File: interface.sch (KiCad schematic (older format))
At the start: 13 parts

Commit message: sch has been finished
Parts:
- removed P?: CONN_10, symbol CONN_10
- removed P?: CONN_01X02, symbol CONN_01X02
- added P11: CONN_1x2, symbol CONN_1x2
- added P6: CONN_10, symbol CONN_10
- P10, P14, P15: renamed from P?; symbol CONN_01X02 -> CONN_01X02-RESCUE-BBBCanFly
- gave numbers to parts that had none: 8
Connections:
- net labels added: I2C2_SCL, LCD_DATA5, MMC1_DAT5, P8, P9, SPI1_DI
- net labels removed: CSN, ECAP0, FSYNC, GDO0, GDO2, GPIO_122, INT, SCL, SCLK, SDA, SI, SO, SPI0_SCLK, VCC
- wire segments 133 -> 143
- no-connect marks 0 -> 72
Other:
- moved on the sheet: P12, P13, P7, P8, P9

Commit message: pcb finished.
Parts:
- removed P10, P14, P15: CONN_01X02, symbol CONN_01X02-RESCUE-BBBCanFly
- removed P11: CONN_1x2, symbol CONN_1x2
- added R6: 200K, Resistors_SMD:R_0805, symbol R
- added R7: 30K, Resistors_SMD:R_0805, symbol R
- P12, P13, P8, P9: footprint (none) -> Pin_Headers:Pin_Header_Straight_1x03
- P3, P4: footprint (none) -> Pin_Headers:Pin_Header_Straight_2x23
- P5: footprint (none) -> Pin_Headers:Pin_Header_Straight_2x05
- P6: footprint (none) -> Pin_Headers:Pin_Header_Straight_1x10
- P7: footprint (none) -> Pin_Headers:Pin_Header_Straight_1x04
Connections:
- net labels added: GPIO_26
- wire segments 143 -> 132
- no-connect marks 72 -> 71
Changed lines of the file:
@@
 GPIO_44
 Text Label 4600 1300 0    60   ~ 0
-EHRPWM1A
+GPIO_26
 Text Label 4600 1400 0    60   ~ 0
 GPIO_46
@@
 F 0 "P7" V 8200 950 50  0000 C CNN
 F 1 "CONN_4" V 8300 950 50  0000 C CNN
-F 2 "" H 8250 950 60  0000 C CNN
+F 2 "Pin_Headers:Pin_Header_Straight_1x04" H 8250 950 60  0001 C CNN
 F 3 "" H 8250 950 60  0000 C CNN
 	1    8250 950
@@
 F 0 "P3" H 1650 3000 50  0000 C CNN
 F 1 "CONN_02X23" V 1650 1800 50  0000 C CNN
-F 2 "" H 1650 950 50  0000 C CNN
+F 2 "Pin_Headers:Pin_Header_Straight_2x23" H 1650 950 50  0001 C CNN
 F 3 "" H 1650 950 50  0000 C CNN
 	1    1650 1800
@@
 F 0 "P4" H 4300 3000 50  0000 C CNN
 F 1 "CONN_02X23" V 4300 1800 50  0000 C CNN
-F 2 "" H 4300 950 50  0000 C CNN
+F 2 "Pin_Headers:Pin_Header_Straight_2x23" H 4300 950 50  0001 C CNN
 F 3 "" H 4300 950 50  0000 C CNN
 	1    4300 1800
@@
 F 0 "P5" H 6550 1200 50  0000 C CNN
 F 1 "CONN_02X05" H 6550 600 50  0001 C CNN
-F 2 "" H 6550 -300 50  0000 C CNN
+F 2 "Pin_Headers:Pin_Header_Straight_2x05" H 6550 -300 50  0001 C CNN
 F 3 "" H 6550 -300 50  0000 C CNN
 	1    6550 900
@@
 Wire Notes Line
 	8400 1500 8400 550
-$Comp
-L CONN_01X02-RESCUE-BBBCanFly P10
-U 1 1 57651A73
-P 9950 850
-AR Path="/57651A73" Ref="P10"  Part="1"
-AR Path="/570FB5F8/57651A73" Ref="P10"  Part="1"
-F 0 "P10" H 9950 1000 50  0000 C CNN
-F 1 "CONN_01X02" V 10050 850 50  0000 C CNN
-F 2 "" H 9950 850 50  0000 C CNN
-F 3 "" H 9950 850 50  0000 C CNN
-	1    9950 850
-	1    0    0    -1
-$EndComp
-$Comp
-L CONN_01X02-RESCUE-BBBCanFly P15
-U 1 1 57651C86
-P 10750 850
-AR Path="/57651C86" Ref="P15"  Part="1"
-AR Path="/570FB5F8/57651C86" Ref="P15"  Part="1"
-F 0 "P15" H 10750 1000 50  0000 C CNN
-F 1 "CONN_01X02" V 10850 850 50  0000 C CNN
-F 2 "" H 10750 850 50  0000 C CNN
-F 3 "" H 10750 850 50  0000 C CNN
-	1    10750 850
-	1    0    0    -1
-$EndComp
-$Comp
-L CONN_01X02-RESCUE-BBBCanFly P14
-U 1 1 57651D39
-P 10700 1450
-AR Path="/57651D39" Ref="P14"  Part="1"
-AR Path="/570FB5F8/57651D39" Ref="P14"  Part="1"
-F 0 "P14" H 10700 1600 50  0000 C CNN
-F 1 "CONN_01X02" V 10800 1450 50  0000 C CNN
-F 2 "" H 10700 1450 50  0000 C CNN
-F 3 "" H 10700 1450 50  0000 C CNN
-	1    10700 1450
-	1    0    0    -1
-$EndComp
-$Comp
-L +24V #PWR7
-U 1 1 57651D88
-P 9550 750
-F 0 "#PWR7" H 9550 600 50  0001 C CNN
-F 1 "+24V" H 9550 890 50  0000 C CNN
-F 2 "" H 9550 750 50  0000 C CNN
-F 3 "" H 9550 750 50  0000 C CNN
-	1    9550 750
-	1    0    0    -1
-$EndComp
-$Comp
-L +24V #PWR15
-U 1 1 57651DAE
-P 10350 1350
-F 0 "#PWR15" H 10350 1200 50  0001 C CNN
-F 1 "+24V" H 10350 1490 50  0000 C CNN
-F 2 "" H 10350 1350 50  0000 C CNN
-F 3 "" H 10350 1350 50  0000 C CNN
-	1    10350 1350
-	1    0    0    -1
-$EndComp
-$Comp
-L +24V #PWR13
-U 1 1 57651E68
-P 10350 750
-F 0 "#PWR13" H 10350 600 50  0001 C CNN
-F 1 "+24V" H 10350 890 50  0000 C CNN
-F 2 "" H 10350 750 50  0000 C CNN
-F 3 "" H 10350 750 50  0000 C CNN
-	1    10350 750
-	1    0    0    -1
-$EndComp
-$Comp
-L +24V #PWR9
-U 1 1 57651E8E
-P 9550 1350
-F 0 "#PWR9" H 9550 1200 50  0001 C CNN
-F 1 "+24V" H 9550 1490 50  0000 C CNN
-F 2 "" H 9550 1350 50  0000 C CNN
-F 3 "" H 9550 1350 50  0000 C CNN
-	1    9550 1350
-	1    0    0    -1
-$EndComp
-Wire Wire Line
-	9450 800  9750 800
-Wire Wire Line
-	10350 800  10550 800
-Wire Wire Line
-	10500 1400 10350 1400
-Wire Wire Line
-	9550 1400 9750 1400
-$Comp
-L GND #PWR8
-U 1 1 57653080
-P 9550 950
-F 0 "#PWR8" H 9550 700 50  0001 C CNN
-F 1 "GND" H 9550 800 50  0000 C CNN
-F 2 "" H 9550 950 50  0000 C CNN
-F 3 "" H 9550 950 50  0000 C CNN
-	1    9550 950
-	1    0    0    -1
-$EndComp
-$Comp
-L GND #PWR14
-U 1 1 576530D8
-P 10350 950
-F 0 "#PWR14" H 10350 700 50  0001 C CNN
-F 1 "GND" H 10350 800 50  0000 C CNN
-F 2 "" H 10350 950 50  0000 C CNN
-F 3 "" H 10350 950 50  0000 C CNN
-	1    10350 950
-	1    0    0    -1
-$EndComp
-$Comp
-L GND #PWR16
-U 1 1 576530FE
-P 10350 1550
-F 0 "#PWR16" H 10350 1300 50  0001 C CNN
-F 1 "GND" H 10350 1400 50  0000 C CNN
-F 2 "" H 10350 1550 50  0000 C CNN
-F 3 "" H 10350 1550 50  0000 C CNN
-	1    10350 1550
-	1    0    0    -1
-$EndComp
-$Comp
-L GND #PWR10
-U 1 1 57653124
-P 9550 1550
-F 0 "#PWR10" H 9550 1300 50  0001 C CNN
-F 1 "GND" H 9550 1400 50  0000 C CNN
-F 2 "" H 9550 1550 50  0000 C CNN
-F 3 "" H 9550 1550 50  0000 C CNN
-	1    9550 1550
-	1    0    0    -1
-$EndComp
-Wire Wire Line
-	10550 900  10350 900
-Wire Wire Line
-	9550 900  9750 900
-Wire Wire Line
-	9750 1500 9550 1500
-Wire Wire Line
-	10350 1500 10500 1500
 $Comp
 L CONN_01X03 P8
@@
 F 0 "P8" H 8800 2400 50  0000 C CNN
 F 1 "CONN_01X03" V 8900 2200 50  0000 C CNN
-F 2 "" H 8800 2200 50  0000 C CNN
+F 2 "Pin_Headers:Pin_Header_Straight_1x03" H 8800 2200 50  0001 C CNN
 F 3 "" H 8800 2200 50  0000 C CNN
 	1    8800 2200
@@
 F 0 "P12" H 10150 2400 50  0000 C CNN
 F 1 "CONN_01X03" V 10250 2200 50  0000 C CNN
-F 2 "" H 10150 2200 50  0000 C CNN
+F 2 "Pin_Headers:Pin_Header_Straight_1x03" H 10150 2200 50  0001 C CNN
 F 3 "" H 10150 2200 50  0000 C CNN
 	1    10150 2200
@@
 F 0 "P9" H 8800 3200 50  0000 C CNN
 F 1 "CONN_01X03" V 8900 3000 50  0000 C CNN
-F 2 "" H 8800 3000 50  0000 C CNN
+F 2 "Pin_Headers:Pin_Header_Straight_1x03" H 8800 3000 50  0001 C CNN
 F 3 "" H 8800 3000 50  0000 C CNN
 	1    8800 3000
@@
 F 0 "P13" H 10150 3200 50  0000 C CNN
 F 1 "CONN_01X03" V 10250 3000 50  0000 C CNN
-F 2 "" H 10150 3000 50  0000 C CNN
+F 2 "Pin_Headers:Pin_Header_Straight_1x03" H 10150 3000 50  0001 C CNN
 F 3 "" H 10150 3000 50  0000 C CNN
 	1    10150 3000
@@
 $EndComp
 $Comp
-L GND #PWR5
+L GND #PWR04
 U 1 1 5765358A
 P 8400 2350
-F 0 "#PWR5" H 8400 2100 50  0001 C CNN
+F 0 "#PWR04" H 8400 2100 50  0001 C CNN
 F 1 "GND" H 8400 2200 50  0000 C CNN
 F 2 "" H 8400 2350 50  0000 C CNN
@@
 $EndComp
 $Comp
-L GND #PWR11
+L GND #PWR05
 U 1 1 576535BC
 P 9800 2350
-F 0 "#PWR11" H 9800 2100 50  0001 C CNN
+F 0 "#PWR05" H 9800 2100 50  0001 C CNN
 F 1 "GND" H 9800 2200 50  0000 C CNN
 F 2 "" H 9800 2350 50  0000 C CNN
@@
 $EndComp
 $Comp
-L GND #PWR6
+L GND #PWR06
 U 1 1 576537B9
 P 8450 3150
-F 0 "#PWR6" H 8450 2900 50  0001 C CNN
+F 0 "#PWR06" H 8450 2900 50  0001 C CNN
 F 1 "GND" H 8450 3000 50  0000 C CNN
 F 2 "" H 8450 3150 50  0000 C CNN
@@
 $EndComp
 $Comp
-L GND #PWR12
+L GND #PWR07
 U 1 1 576537EB
 P 9800 3100
-F 0 "#PWR12" H 9800 2850 50  0001 C CNN
+F 0 "#PWR07" H 9800 2850 50  0001 C CNN
 F 1 "GND" H 9800 2950 50  0000 C CNN
 F 2 "" H 9800 3100 50  0000 C CNN
@@
 Text Label 8100 2900 0    60   ~ 0
 EHRPWM2A
-Text HLabel 9450 800  0    60   Input ~ 0
-24V
 Text Label 4250 3100 0    60   ~ 0
 P8
@@
 ECAPPWM0
 $Comp
-L GND #PWR4
+L GND #PWR08
 U 1 1 57B1CADA
 P 6250 1900
-F 0 "#PWR4" H 6250 1650 50  0001 C CNN
+F 0 "#PWR08" H 6250 1650 50  0001 C CNN
 F 1 "GND" H 6250 1750 50  0000 C CNN
 F 2 "" H 6250 1900 50  0000 C CNN
@@
 NoConn ~ 750  2400
 NoConn ~ 750  2500
-NoConn ~ 750  2600
 NoConn ~ 750  2700
 NoConn ~ 2550 2600
@@
 	8400 2350 8400 2300
 Wire Wire Line
-	9550 950  9550 900
-Wire Wire Line
-	10350 900  10350 950
-Wire Wire Line
 	8450 3100 8450 3150
 Wire Wire Line
 	9800 2300 9800 2350
-Wire Wire Line
-	9550 1400 9550 1350
-Wire Wire Line
-	9550 1500 9550 1550
-Wire Wire Line
-	10350 1550 10350 1500
-Wire Wire Line
-	10350 1400 10350 1350
-Wire Wire Line
-	9550 800  9550 750
-Wire Wire Line
-	10350 800  10350 750
 Text Label 6350 2700 0    60   ~ 0
 DGND
 Wire Wire Line
 	6750 2700 6350 2700
-Connection ~ 9550 800
-$Comp
-L CONN_1x2 P11
-U 1 1 57B257AC
-P 10000 1300
-F 0 "P11" H 9950 1300 60  0000 C CNN
-F 1 "CONN_1x2" V 10100 1150 60  0000 C CNN
-F 2 "" H 10000 1300 60  0000 C CNN
-F 3 "" H 10000 1300 60  0000 C CNN
-	1    10000 1300
-	1    0    0    -1
-$EndComp
 $Comp
 L CONN_10 P6
@@
 F 0 "P6" V 6950 1250 60  0000 C CNN
 F 1 "CONN_10" V 7050 1250 60  0000 C CNN
-F 2 "" H 7000 1750 60  0000 C CNN
+F 2 "Pin_Headers:Pin_Header_Straight_1x10" H 7000 1750 60  0001 C CNN
 F 3 "" H 7000 1750 60  0000 C CNN
 	1    7000 1750
 	1    0    0    -1
 $EndComp
+$Comp
+L +24V #PWR09
+U 1 1 57CD415B
+P 9000 700
+F 0 "#PWR09" H 9000 550 50  0001 C CNN
+F 1 "+24V" H 9000 840 50  0000 C CNN
+F 2 "" H 9000 700 50  0000 C CNN
+F 3 "" H 9000 700 50  0000 C CNN
+	1    9000 700
+	1    0    0    -1
+$EndComp
+$Comp
+L GND #PWR010
+U 1 1 57CD418D
+P 9000 1550
+F 0 "#PWR010" H 9000 1300 50  0001 C CNN
+F 1 "GND" H 9000 1400 50  0000 C CNN
+F 2 "" H 9000 1550 50  0000 C CNN
+F 3 "" H 9000 1550 50  0000 C CNN
+	1    9000 1550
+	1    0    0    -1
+$EndComp
+$Comp
+L R R6
+U 1 1 57CD41E5
+P 9000 950
+F 0 "R6" V 9080 950 50  0000 C CNN
+F 1 "200K" V 9000 950 50  0000 C CNN
+F 2 "Resistors_SMD:R_0805" V 8930 950 50  0001 C CNN
+F 3 "" H 9000 950 50  0000 C CNN
+	1    9000 950
+	1    0    0    -1
+$EndComp
+$Comp
+L R R7
+U 1 1 57CD4260
+P 9000 1350
+F 0 "R7" V 9080 1350 50  0000 C CNN
+F 1 "30K" V 9000 1350 50  0000 C CNN
+F 2 "Resistors_SMD:R_0805" V 8930 1350 50  0001 C CNN
+F 3 "" H 9000 1350 50  0000 C CNN
+	1    9000 1350
+	1    0    0    -1
+$EndComp
+Wire Wire Line
+	9000 700  9000 800
+Wire Wire Line
+	9000 1100 9000 1200
+Wire Wire Line
+	9000 1500 9000 1550
+Wire Wire Line
+	9000 1150 8650 1150
+Connection ~ 9000 1150
+Text Label 8650 1150 0    60   ~ 0
+AIN0
+Wire Wire Line
+	8750 750  9000 750
+Connection ~ 9000 750
+Text HLabel 8750 750  0    60   Input ~ 0
+24V
 $EndSCHEMATC

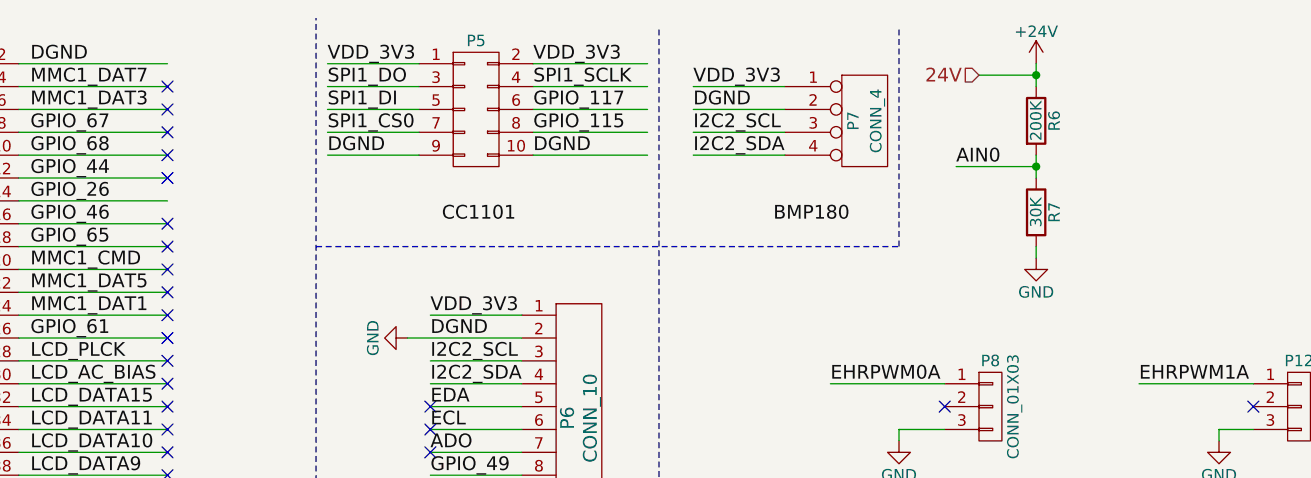
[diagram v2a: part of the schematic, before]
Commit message: modified power supply program
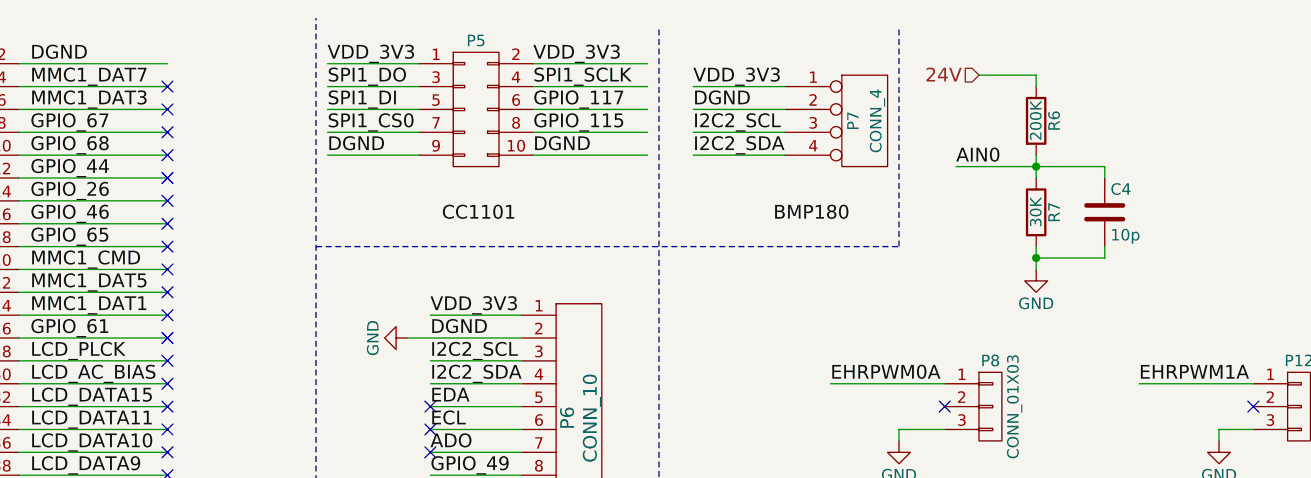
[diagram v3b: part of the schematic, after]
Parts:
- added C4: 10p, Capacitors_SMD:C_0805_HandSoldering, symbol C
- R6, R7: footprint Resistors_SMD:R_0805 -> Resistors_SMD:R_0805_HandSoldering
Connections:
- net labels removed: +24V
- wire segments 132 -> 135
- no-connect marks 71 -> 72
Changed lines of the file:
@@
 $EndComp
 $Comp
-L GND #PWR04
+L GND #PWR05
 U 1 1 5765358A
 P 8400 2350
-F 0 "#PWR04" H 8400 2100 50  0001 C CNN
+F 0 "#PWR05" H 8400 2100 50  0001 C CNN
 F 1 "GND" H 8400 2200 50  0000 C CNN
 F 2 "" H 8400 2350 50  0000 C CNN
@@
 $EndComp
 $Comp
-L GND #PWR05
+L GND #PWR06
 U 1 1 576535BC
 P 9800 2350
-F 0 "#PWR05" H 9800 2100 50  0001 C CNN
+F 0 "#PWR06" H 9800 2100 50  0001 C CNN
 F 1 "GND" H 9800 2200 50  0000 C CNN
 F 2 "" H 9800 2350 50  0000 C CNN
@@
 $EndComp
 $Comp
-L GND #PWR06
+L GND #PWR07
 U 1 1 576537B9
 P 8450 3150
-F 0 "#PWR06" H 8450 2900 50  0001 C CNN
+F 0 "#PWR07" H 8450 2900 50  0001 C CNN
 F 1 "GND" H 8450 3000 50  0000 C CNN
 F 2 "" H 8450 3150 50  0000 C CNN
@@
 $EndComp
 $Comp
-L GND #PWR07
+L GND #PWR08
 U 1 1 576537EB
 P 9800 3100
-F 0 "#PWR07" H 9800 2850 50  0001 C CNN
+F 0 "#PWR08" H 9800 2850 50  0001 C CNN
 F 1 "GND" H 9800 2950 50  0000 C CNN
 F 2 "" H 9800 3100 50  0000 C CNN
@@
 ECAPPWM0
 $Comp
-L GND #PWR08
+L GND #PWR09
 U 1 1 57B1CADA
 P 6250 1900
-F 0 "#PWR08" H 6250 1650 50  0001 C CNN
+F 0 "#PWR09" H 6250 1650 50  0001 C CNN
 F 1 "GND" H 6250 1750 50  0000 C CNN
 F 2 "" H 6250 1900 50  0000 C CNN
@@
 $EndComp
 $Comp
-L +24V #PWR09
-U 1 1 57CD415B
-P 9000 700
-F 0 "#PWR09" H 9000 550 50  0001 C CNN
-F 1 "+24V" H 9000 840 50  0000 C CNN
-F 2 "" H 9000 700 50  0000 C CNN
-F 3 "" H 9000 700 50  0000 C CNN
-	1    9000 700
-	1    0    0    -1
-$EndComp
-$Comp
 L GND #PWR010
 U 1 1 57CD418D
-P 9000 1550
-F 0 "#PWR010" H 9000 1300 50  0001 C CNN
-F 1 "GND" H 9000 1400 50  0000 C CNN
-F 2 "" H 9000 1550 50  0000 C CNN
-F 3 "" H 9000 1550 50  0000 C CNN
-	1    9000 1550
+P 9000 1600
+F 0 "#PWR010" H 9000 1350 50  0001 C CNN
+F 1 "GND" H 9000 1450 50  0000 C CNN
+F 2 "" H 9000 1600 50  0000 C CNN
+F 3 "" H 9000 1600 50  0000 C CNN
+	1    9000 1600
 	1    0    0    -1
 $EndComp
@@
 F 0 "R6" V 9080 950 50  0000 C CNN
 F 1 "200K" V 9000 950 50  0000 C CNN
-F 2 "Resistors_SMD:R_0805" V 8930 950 50  0001 C CNN
+F 2 "Resistors_SMD:R_0805_HandSoldering" V 8930 950 50  0001 C CNN
 F 3 "" H 9000 950 50  0000 C CNN
 	1    9000 950
@@
 F 0 "R7" V 9080 1350 50  0000 C CNN
 F 1 "30K" V 9000 1350 50  0000 C CNN
-F 2 "Resistors_SMD:R_0805" V 8930 1350 50  0001 C CNN
+F 2 "Resistors_SMD:R_0805_HandSoldering" V 8930 1350 50  0001 C CNN
 F 3 "" H 9000 1350 50  0000 C CNN
 	1    9000 1350
@@
 $EndComp
 Wire Wire Line
-	9000 700  9000 800
-Wire Wire Line
 	9000 1100 9000 1200
 Wire Wire Line
-	9000 1500 9000 1550
-Wire Wire Line
-	9000 1150 8650 1150
+	9000 1500 9000 1600
+Wire Wire Line
+	8650 1150 9300 1150
 Connection ~ 9000 1150
 Text Label 8650 1150 0    60   ~ 0
 AIN0
-Wire Wire Line
-	8750 750  9000 750
-Connection ~ 9000 750
 Text HLabel 8750 750  0    60   Input ~ 0
 24V
+NoConn ~ 5200 1300
+Wire Wire Line
+	9000 750  9000 800
+$Comp
+L C C4
+U 1 1 58A9AF91
+P 9300 1350
+F 0 "C4" H 9325 1450 50  0000 L CNN
+F 1 "10p" H 9325 1250 50  0000 L CNN
+F 2 "Capacitors_SMD:C_0805_HandSoldering" H 9338 1200 50  0001 C CNN
+F 3 "" H 9300 1350 50  0000 C CNN
+	1    9300 1350
+	1    0    0    -1
+$EndComp
+Connection ~ 9000 1550
+Wire Wire Line
+	8750 750  9000 750
+Wire Wire Line
+	9300 1150 9300 1200
+Wire Wire Line
+	9300 1500 9300 1550
+Wire Wire Line
+	9300 1550 9000 1550
 $EndSCHEMATC
